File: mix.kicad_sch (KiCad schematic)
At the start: 65 parts, among them J1 Conn_02x05_Odd_Even, J2 AudioJack2_SwitchT, J3 AudioJack2_SwitchT, J4 AudioJack2_SwitchT, J5 AudioJack2_SwitchT, J6 AudioJack2, Q1 BCM847, Q2 BCM847, U1 TL074, U2 TL072

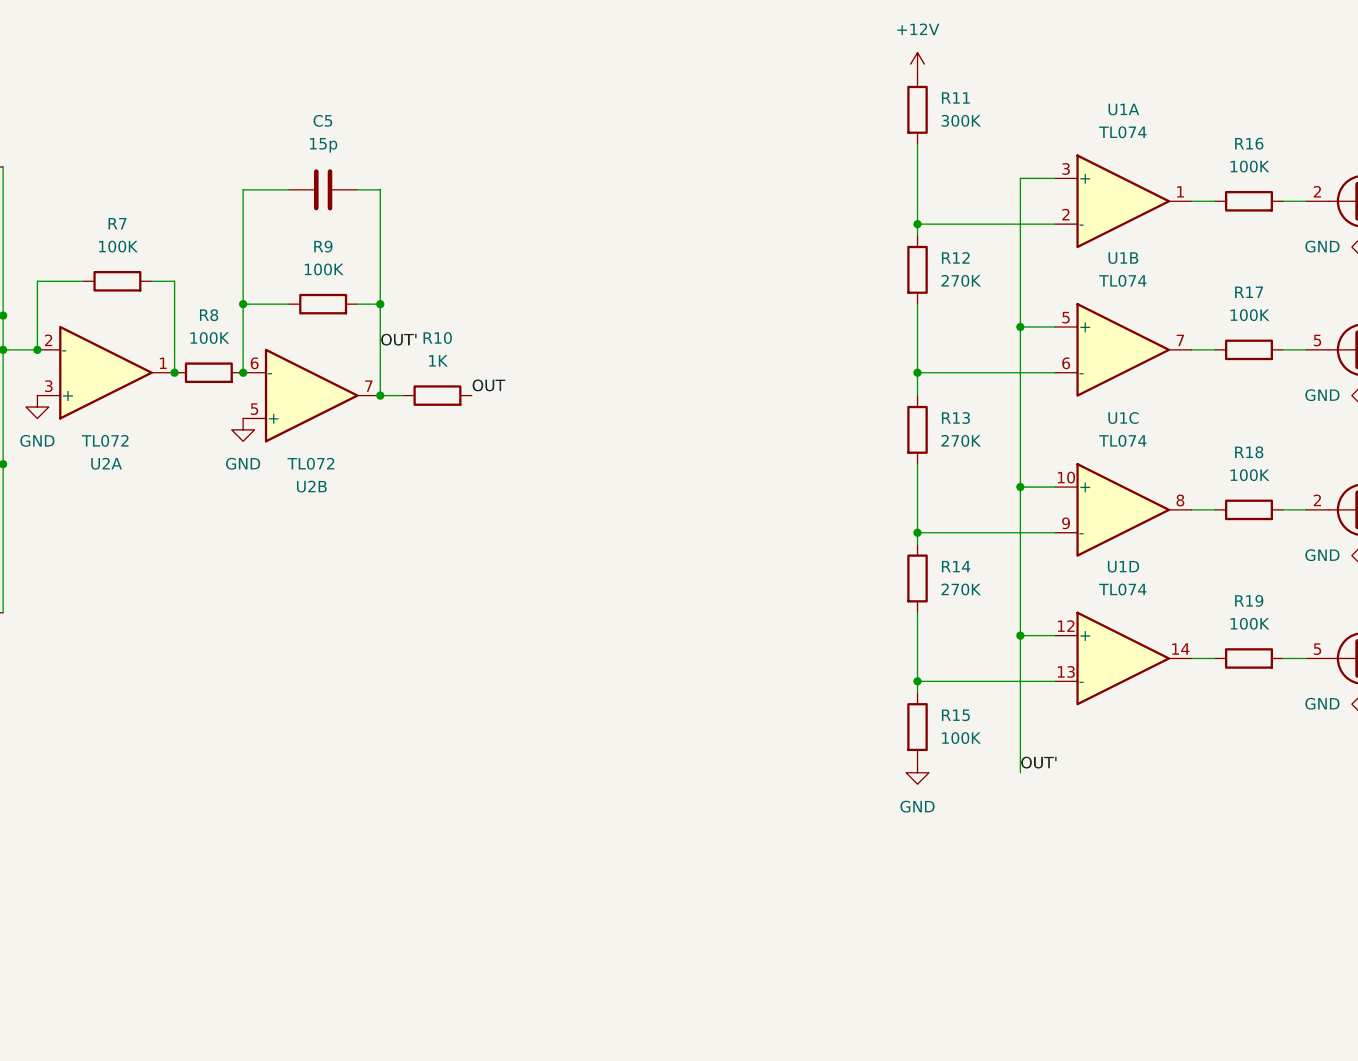
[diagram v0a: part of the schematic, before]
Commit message: adding pcb to readme
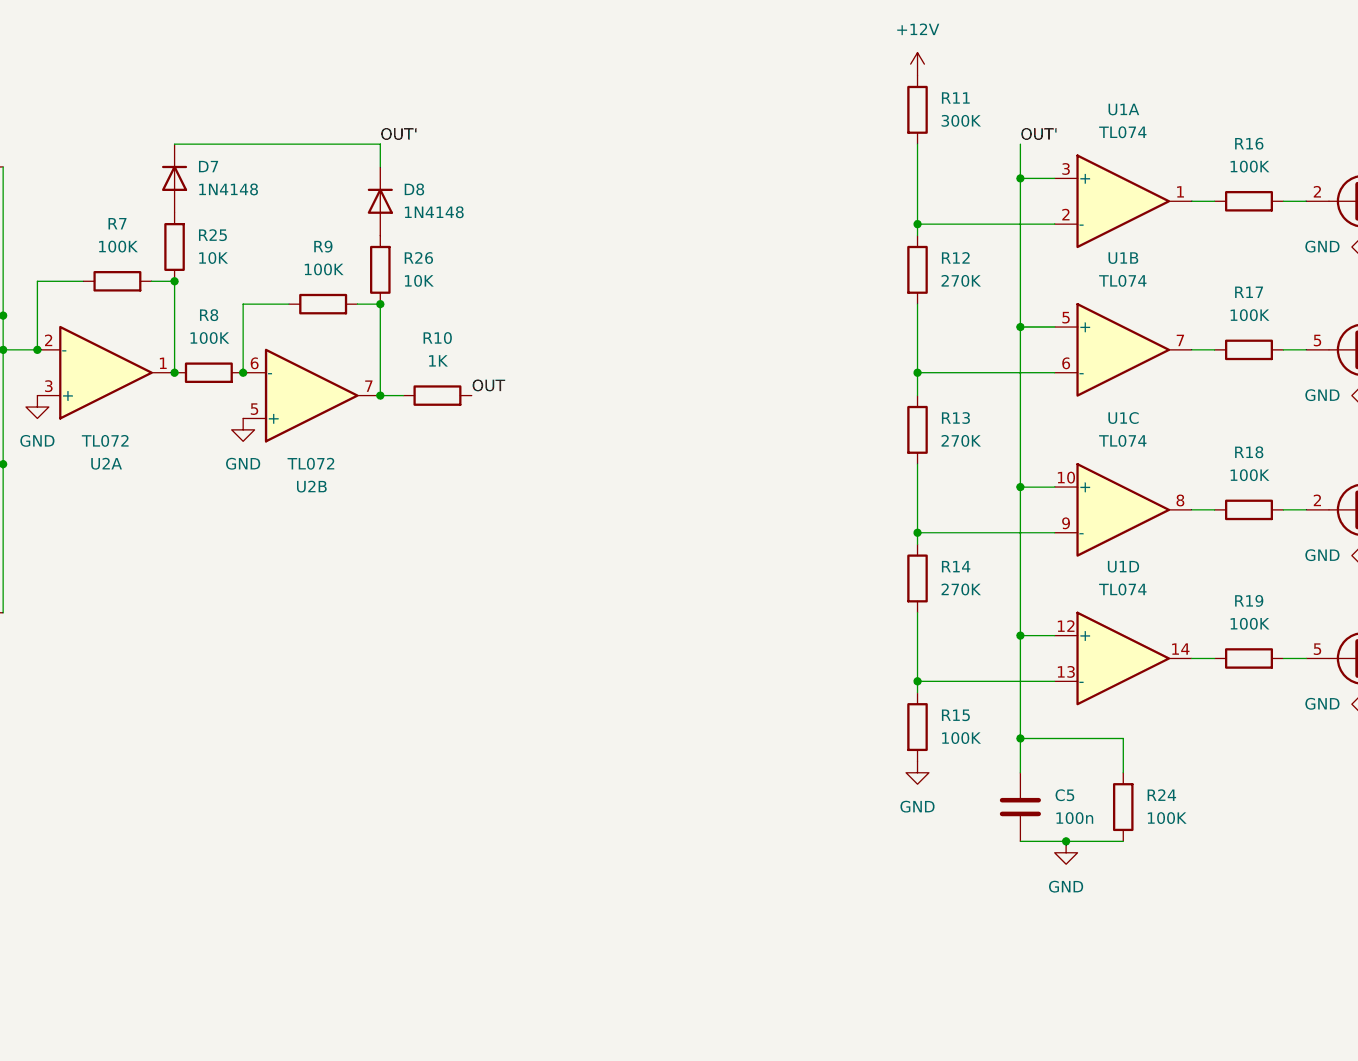
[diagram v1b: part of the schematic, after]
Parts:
- added D7, D8: 1N4148, Diode_SMD:D_SOD-323_HandSoldering, symbol Device:D
- added R24: 100K, Resistor_SMD:R_0805_2012Metric, symbol Device:R
- added R25, R26: 10K, Resistor_SMD:R_0805_2012Metric, symbol Device:R
- C5: value 15p -> 100n
- H5, H6, H7, H8: footprint Eurorack:Mech-AudioJack-Hole -> Eurorack:Mech-AudioJack-Hole-Input
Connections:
- net GND: now also C5.2, R24.1
- net OUT': now also D7.1 (K), D8.1 (K), R24.2; no longer R10.1, R9.2, U2.7
- net at R8.2, R9.1, U2.6 (-): no longer C5.2
- net at R7.2, R8.1, U2.1: now also R25.1
- new net: R10.1, R26.1, R9.2, U2.7
- new net: D7.2 (A), R25.2
- new net: D8.2 (A), R26.2
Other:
- moved on the sheet: C5
